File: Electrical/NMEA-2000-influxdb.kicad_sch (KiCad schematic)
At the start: 10 parts, among them J1 Conn_01x02, J2 Conn_01x02, U1 SD-Card-Module, U2 LM7805_TO220, U3 ESP32-DevKitC, U4 SN65HVD230, U5 RTC-Module

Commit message: Added external connectors
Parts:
- removed J1: Conn_01x02, Capacitor_THT:CP_Radial_D8.0mm_P5.00mm, symbol Connector_Generic:Conn_01x02
- removed J2: Conn_01x02, TerminalBlock_Phoenix:TerminalBlock_Phoenix_MKDS-1,5-2-5.08_1x02_P5.08mm_Horizontal, symbol Connector_Generic:Conn_01x02
- removed U3: ESP32-DevKitC, Espressif:MODULE_ESP32_NODEMCU, symbol Espressif:ESP32-DevKitC
- added J1: Conn_01x04, TerminalBlock_Phoenix:TerminalBlock_Phoenix_MKDS-1,5-4-5.08_1x04_P5.08mm_Horizontal, symbol Connector_Generic:Conn_01x04
- added J2: Conn_01x04, Connector_PinSocket_2.54mm:PinSocket_1x04_P2.54mm_Horizontal, symbol Connector_Generic:Conn_01x04
- added U3: ESP32_NODEMCU, esp32:esp32, symbol ESP32_NODEMCU:ESP32_NODEMCU
- U1, U5: footprint Connector_PinSocket_2.54mm:PinSocket_1x06_P2.54mm_Vertical -> Connector_PinSocket_2.54mm:PinSocket_1x06_P2.54mm_Horizontal
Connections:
- net +12V: now also J1.1 (Pin_1)
- net +3V3: now also U3.19 (3V3)
- net +5V: now also J2.1 (Pin_1), U3.1 (5V)
- net CAN_RX: now also U3.29 (G5)
- net CAN_TX: now also U3.26 (G4)
- net CS: now also U3.8 (G14)
- net GND: now also J1.4 (Pin_4), J2.4 (Pin_4), U3.32 (GND_J4_7), U3.38 (GND_J5_6), U3.6 (GND_J4_1)
- net MISO: now also U3.3 (SD3)
- net MOSI: now also U3.4 (SD2)
- net SCK: now also U3.21 (SD0)
- net SCL: now also U3.5 (G13)
- net SDA: now also U3.7 (G12)
- net CAN_L: now reaches U4.6 (CANL)
- net CAN_L: now also J1.2 (Pin_2)
- net CAN_H: now reaches U4.7 (CANH)
- net CAN_H: now also J1.3 (Pin_3)
- new net RX: J2.2 (Pin_2), U3.34 (RXD)
- new net TX: J2.3 (Pin_3), U3.35 (TXD)

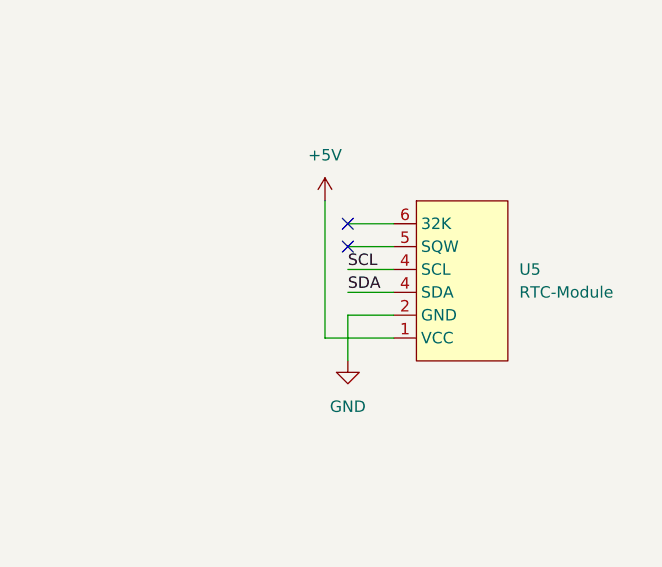
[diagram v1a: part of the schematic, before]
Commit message: Updated board and added heatsink
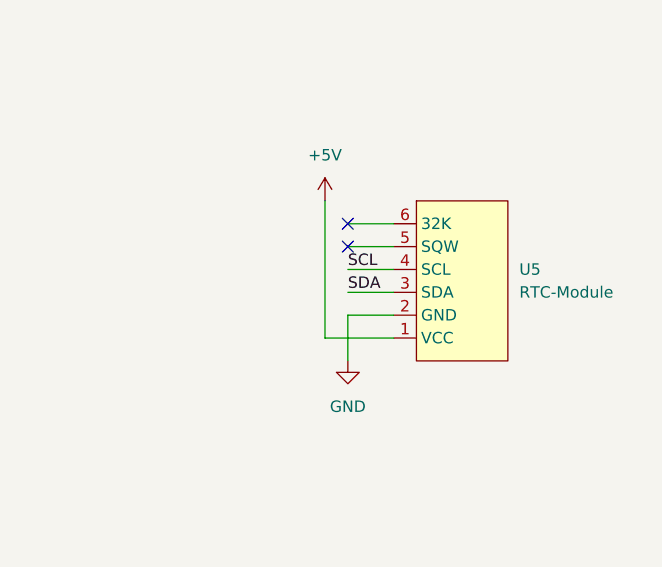
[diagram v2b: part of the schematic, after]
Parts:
- U2: footprint Package_TO_SOT_THT:TO-220-3_Vertical -> Heatsinks:Heatsink_TO220-3_30x25x25mm
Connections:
- net SDA: now also U5.3 (SDA); no longer U5.4 (SDA)

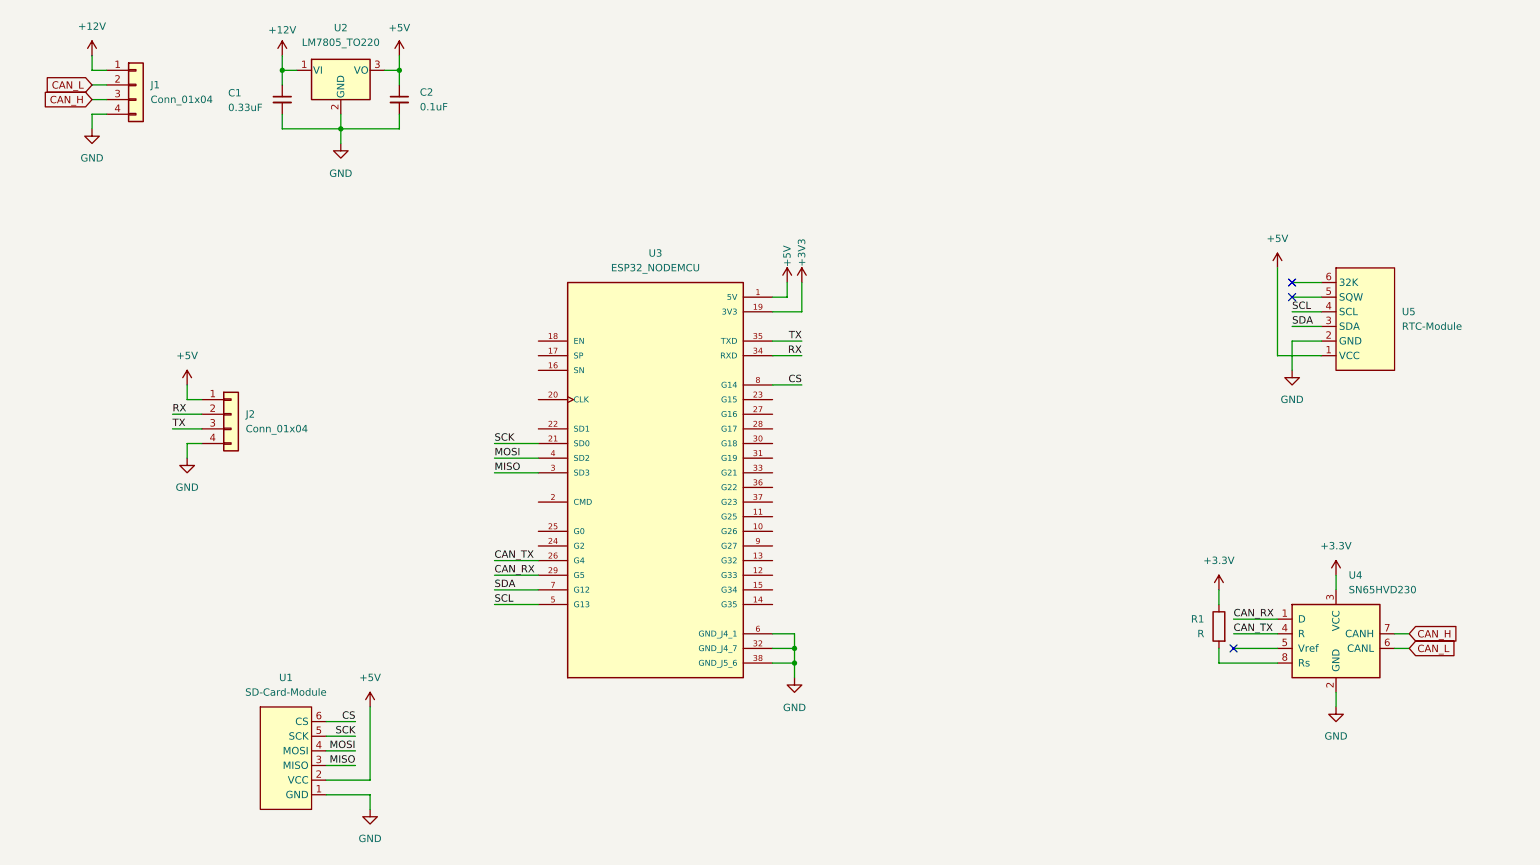
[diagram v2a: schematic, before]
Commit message: Added Seven segment displays
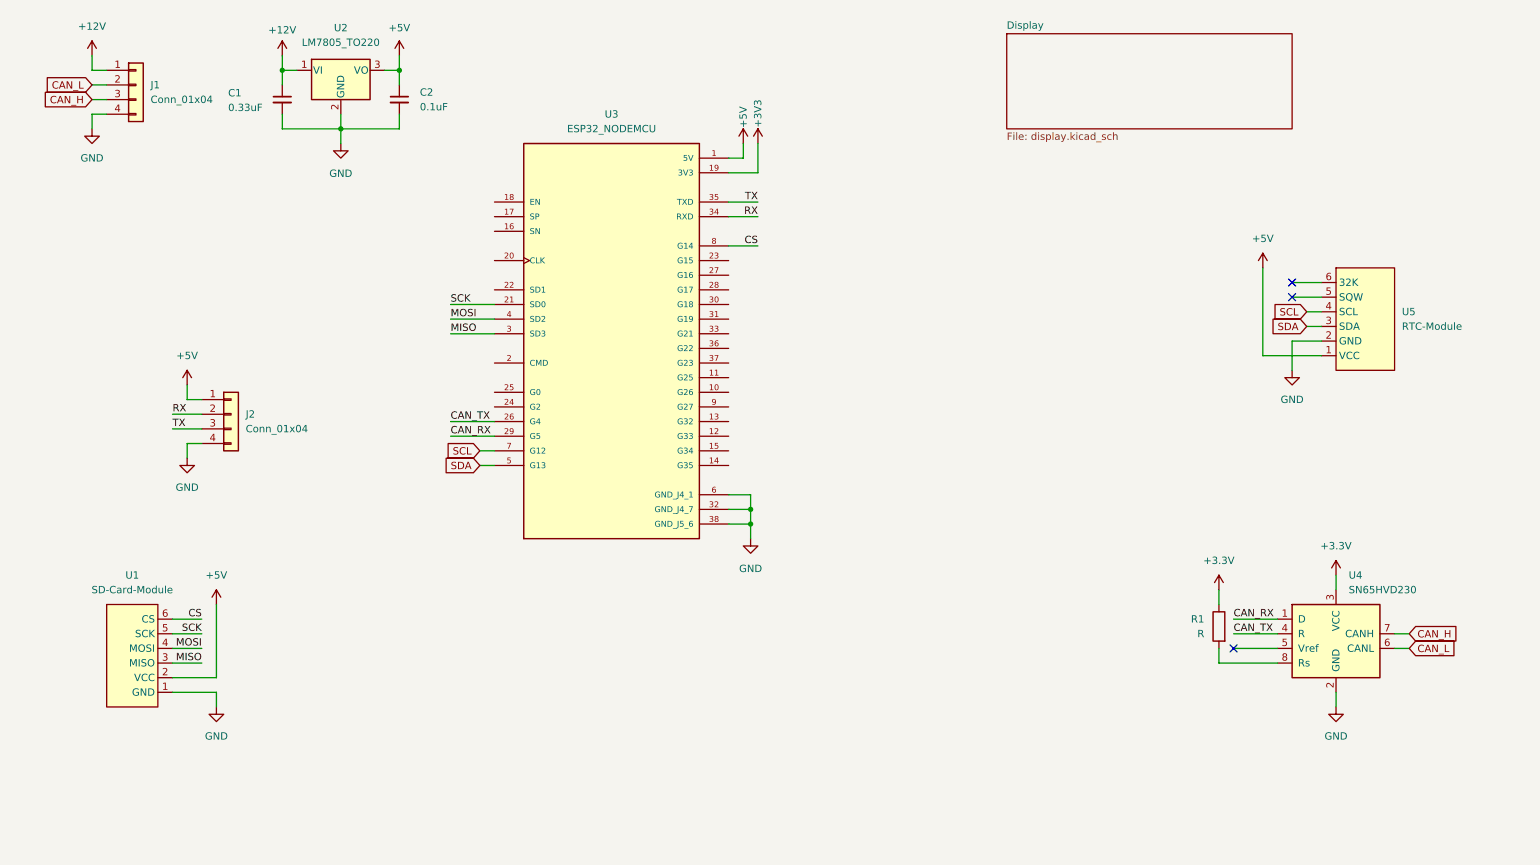
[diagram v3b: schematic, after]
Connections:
- net SCL: now also U3.7 (G12); no longer U3.5 (G13)
- net SDA: now also U3.5 (G13); no longer U3.7 (G12)
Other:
- added sheet Display (display.kicad_sch)
- moved on the sheet: U1, U3

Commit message: Added Alphanumeric display
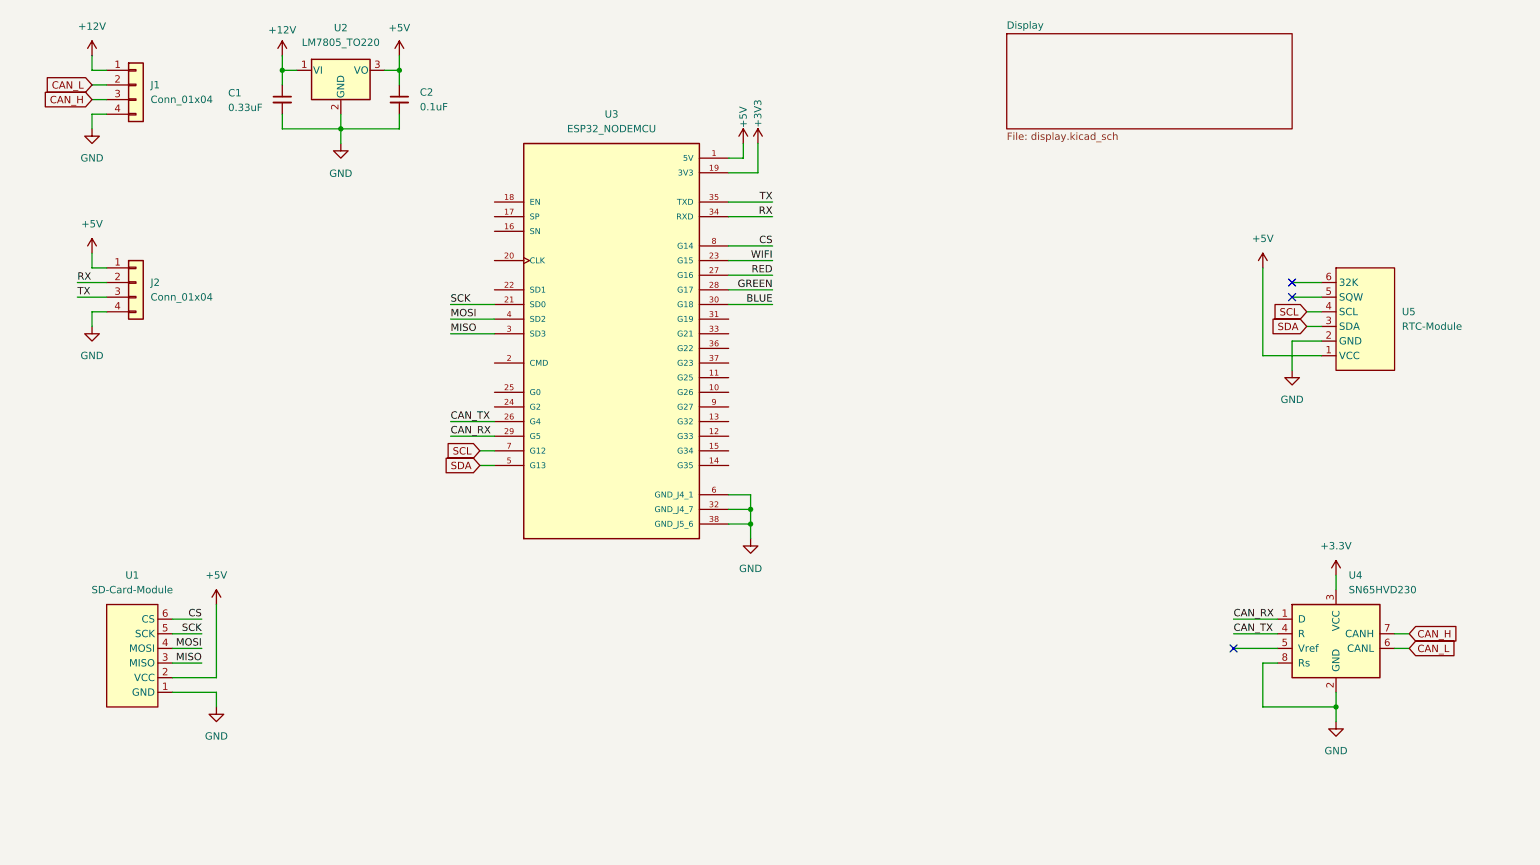
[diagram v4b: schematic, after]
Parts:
- removed R1: R, Resistor_THT:R_Axial_DIN0204_L3.6mm_D1.6mm_P5.08mm_Horizontal, symbol Device:R
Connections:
- net GND: now also U4.8 (Rs)
- net WIFI: now reaches U3.23 (G15)
- net RED: now reaches U3.27 (G16)
- net GREEN: now reaches U3.28 (G17)
- net BLUE: now reaches U3.30 (G18)
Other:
- moved on the sheet: J2

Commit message: Added Display PCB
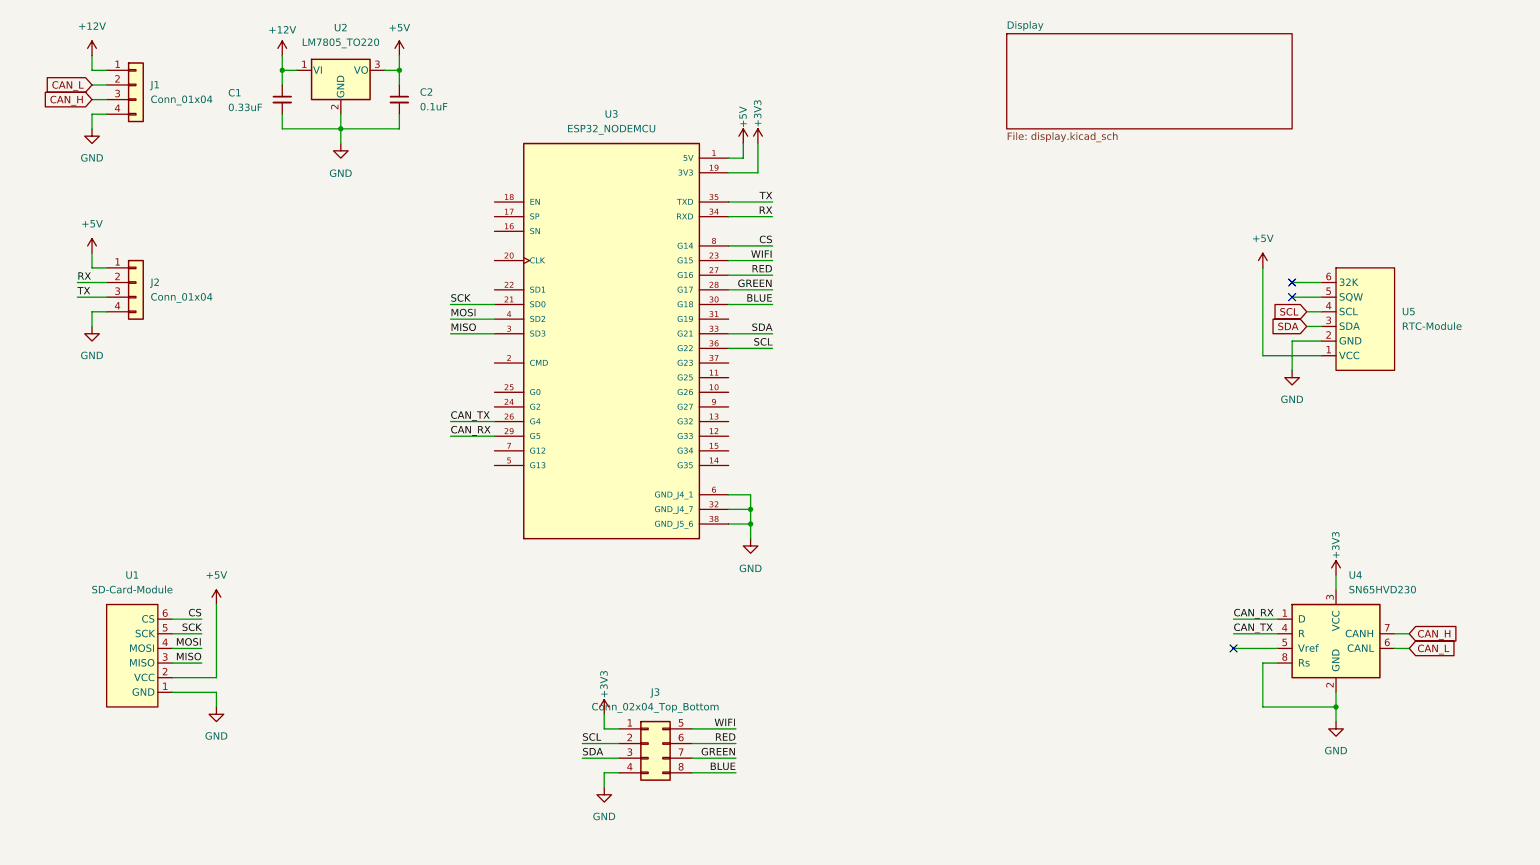
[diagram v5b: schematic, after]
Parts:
- added J3: Conn_02x04_Top_Bottom, Connector_IDC:IDC-Header_2x04_P2.54mm_Vertical, symbol Connector_Generic:Conn_02x04_Top_Bottom
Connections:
- net +3.3V is gone; now on net +3V3: U4.3 (VCC)
- net +3V3: now also J3.1 (Pin_1)
- net BLUE: now also J3.8 (Pin_8)
- net GND: now also J3.4 (Pin_4)
- net GREEN: now also J3.7 (Pin_7)
- net RED: now also J3.6 (Pin_6)
- net SCL: now also U3.36 (G22), J3.2 (Pin_2); no longer U3.7 (G12)
- net SDA: now also U3.33 (G21), J3.3 (Pin_3); no longer U3.5 (G13)
- net WIFI: now also J3.5 (Pin_5)

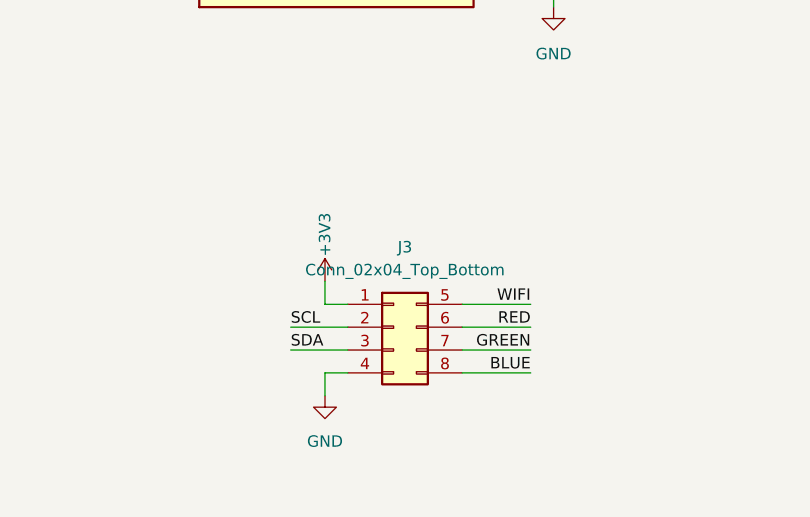
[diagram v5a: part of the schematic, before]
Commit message: Updated Display
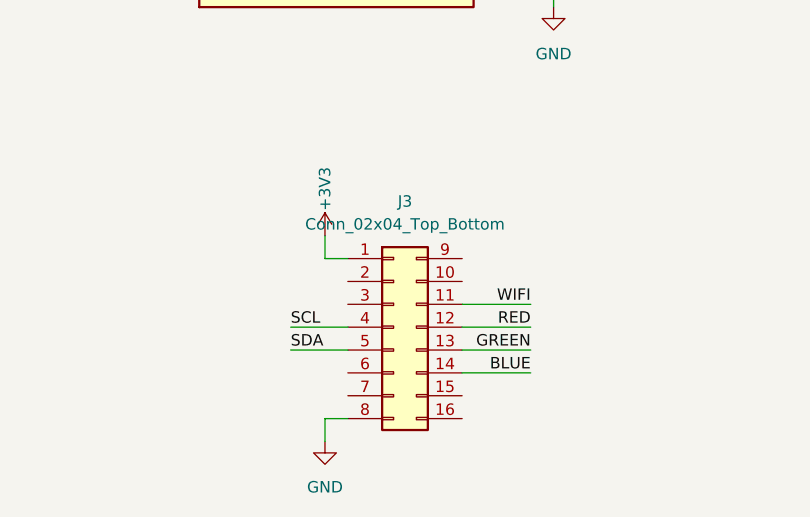
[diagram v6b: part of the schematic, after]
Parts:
- J3: footprint Connector_IDC:IDC-Header_2x04_P2.54mm_Vertical -> Connector_IDC:IDC-Header_2x08_P2.54mm_Vertical; symbol Connector_Generic:Conn_02x04_Top_Bottom -> Connector_Generic:Conn_02x08_Top_Bottom
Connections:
- net BLUE: now also J3.14 (Pin_14); no longer J3.8 (Pin_8)
- net GND: now also J3.8 (Pin_8); no longer J3.4 (Pin_4)
- net GREEN: now also J3.13 (Pin_13); no longer J3.7 (Pin_7)
- net RED: now also J3.12 (Pin_12); no longer J3.6 (Pin_6)
- net SCL: now also J3.4 (Pin_4); no longer J3.2 (Pin_2)
- net SDA: now also J3.5 (Pin_5); no longer J3.3 (Pin_3)
- net WIFI: now also J3.11 (Pin_11); no longer J3.5 (Pin_5)

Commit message: Updated schematic
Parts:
- added JP10: Jumper_2_Open, Connector_PinHeader_2.54mm:PinHeader_1x02_P2.54mm_Vertical, symbol Jumper:Jumper_2_Open
- added JP11: Jumper_3_Bridged12, Connector_PinHeader_2.54mm:PinHeader_1x03_P2.54mm_Vertical, symbol Jumper:Jumper_3_Bridged12
- added R19: 120R, Resistor_THT:R_Axial_DIN0204_L3.6mm_D1.6mm_P5.08mm_Horizontal, symbol Device:R_Small
- J3: value Conn_02x04_Top_Bottom -> Conn_02x04
- renumbered U2 to U1, U3 to U2, U5 to U3, U1 to U4, U4 to U5
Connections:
- net +3V3: now also J3.2 (Pin_2), JP11.3 (B); no longer J3.1 (Pin_1)
- net +5V: now also J3.1 (Pin_1)
- net BLUE: now also J3.15 (Pin_15); no longer J3.14 (Pin_14)
- net CAN_H: now also J1.2 (Pin_2), J3.3 (Pin_3), U5.6 (CANL), R19.2; no longer J1.3 (Pin_3), U5.7 (CANH)
- net CAN_L: now also J1.3 (Pin_3), J3.4 (Pin_4), U5.7 (CANH), JP10.2 (B); no longer J1.2 (Pin_2), U5.6 (CANL)
- net GND: now also J3.16 (Pin_16), JP11.1 (A); no longer J3.8 (Pin_8), U5.8 (Rs)
- net GREEN: now also J3.14 (Pin_14); no longer J3.13 (Pin_13)
- net RED: now also J3.13 (Pin_13); no longer J3.12 (Pin_12)
- net SCL: now also J3.5 (Pin_5); no longer J3.4 (Pin_4)
- net SDA: now also J3.6 (Pin_6); no longer J3.5 (Pin_5)
- net SW_CY: now reaches U2.10 (G26)
- net SW_CY: now also J3.8 (Pin_8)
- net SD_ST: now reaches U2.11 (G25)
- net SD_ST: now also J3.10 (Pin_10)
- net CAN_ST: now reaches U2.31 (G19)
- net CAN_ST: now also J3.9 (Pin_9)
- net RTC_ST: now reaches U2.37 (G23)
- net RTC_ST: now also J3.11 (Pin_11)
- net SW_TG: now reaches U2.9 (G27)
- net SW_TG: now also J3.7 (Pin_7)
- net WIFI renamed WIFI_ST
- net WIFI_ST: now also J3.12 (Pin_12); no longer J3.11 (Pin_11)
- new net: JP10.1 (A), R19.1
- new net: JP11.2 (C), U5.8 (Rs)
- no-connect marks 3 -> 10
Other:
- moved on the sheet: C1, C2, J1, J2, U1, U3, U4, U5
